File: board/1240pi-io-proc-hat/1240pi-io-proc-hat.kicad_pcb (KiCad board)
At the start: 2 copper layers, 29.2 x 63.5 mm, 12 parts, among them J1 62684-50210, J2 SFV10R-1ST, P445 Header, U445 Z80

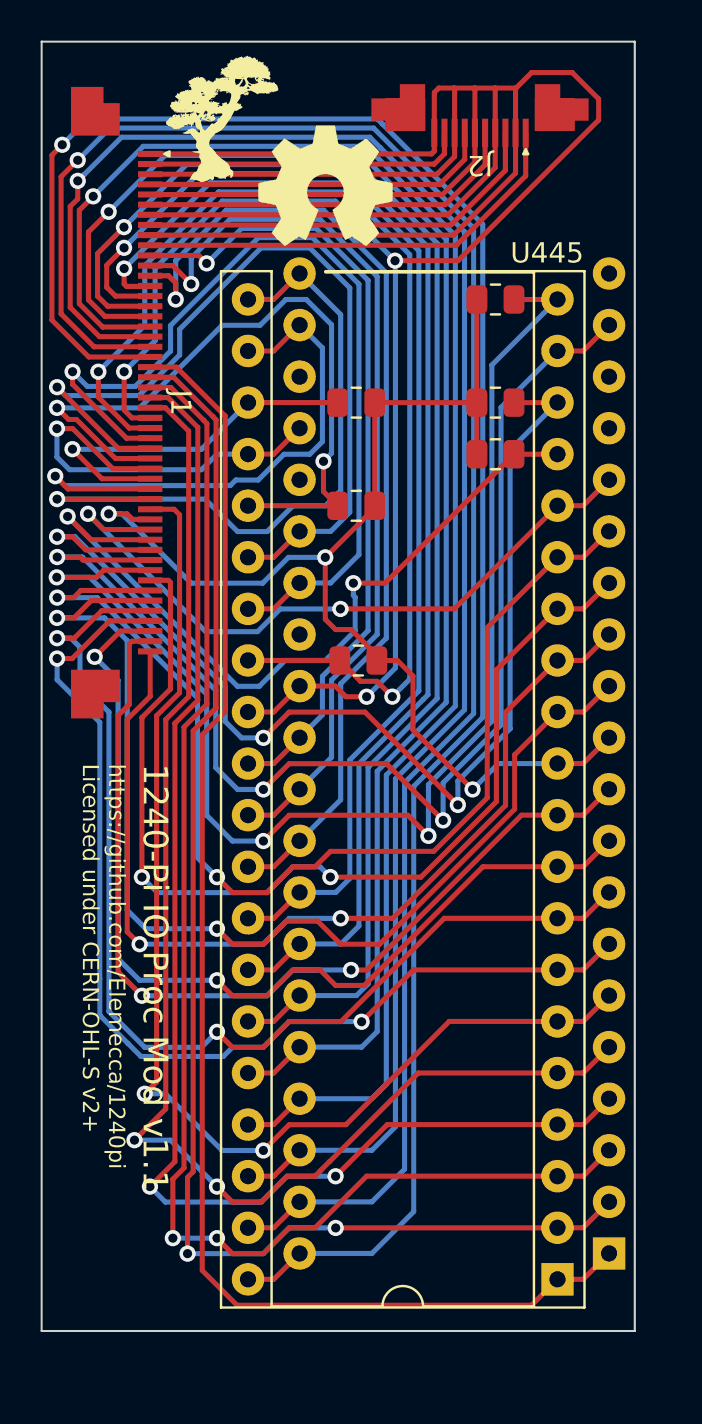
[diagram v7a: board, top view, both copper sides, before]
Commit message: Rearrange IO Proc hat, add IO Proc interface.
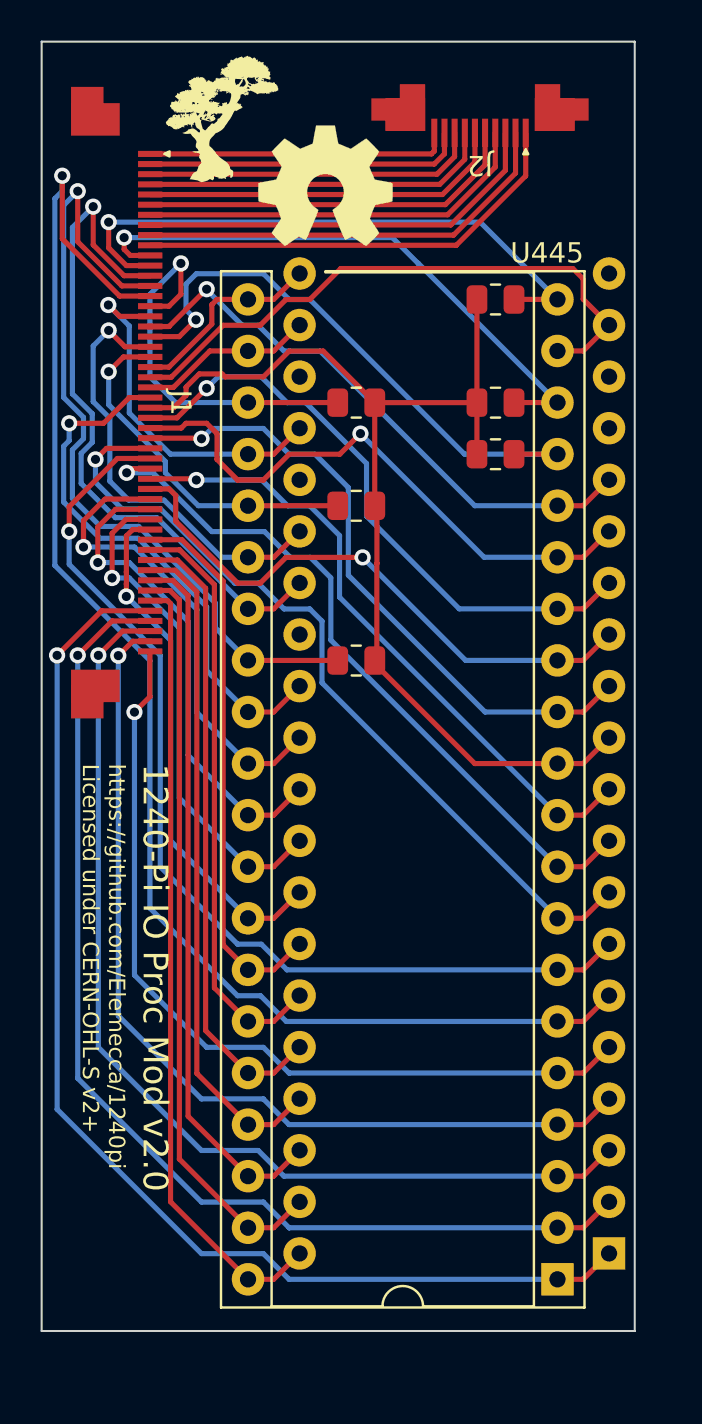
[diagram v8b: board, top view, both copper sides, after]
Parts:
- moved R2 0.10 mm to (150.1, 71.1)
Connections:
- net /~{VDRIVE} renamed /VDRIVE_GREEN
- J1 pad 1: GND -> /VGND5
- J1 pad 11: /A0 -> /~{HALT}
- J1 pad 12: /A1 -> /~{IORQ}
- J1 pad 13: /A2 -> /~{M1}
- J1 pad 14: /A3 -> /~{RFSH}
- J1 pad 15: /A4 -> /~{CLK}
- J1 pad 16: /A5 -> /~{BUSACK}
- J1 pad 17: /A6 -> /~{WAIT}
- J1 pad 18: /A7 -> /~{INT}
- J1 pad 19: /A8 -> /~{NMI}
- J1 pad 20: /A9 -> /~{RESET}
- J1 pad 21: /A10 -> /~{BUSREQ}
- J1 pad 22: /A11 -> /~{RD}
- J1 pad 23: /A12 -> /~{MREQ}
- J1 pad 24: /A13 -> /~{WR}
- J1 pad 25: /A14 -> GND
- J1 pad 26: /A15 -> +5V
- J1 pad 27: GND -> /D0
- J1 pad 28: /~{RFSH} -> /D1
- J1 pad 29: /~{M1} -> /D2
- J1 pad 3: GND -> /VGND4
- J1 pad 30: /~{RESET} -> /D3
- J1 pad 31: /~{BUSRQ} -> /D4
- J1 pad 32: /~{WAIT} -> /D5
- J1 pad 33: /~{BUSACK} -> /D6
- J1 pad 34: /~{WR} -> /D7
- J1 pad 35: /~{RD} -> /A0
- J1 pad 36: /~{CLK} -> /A1
- J1 pad 37: +5V -> /A2
- J1 pad 38: /~{INT} -> /A3
- J1 pad 39: /~{NMI} -> /A4
- J1 pad 40: /~{HALT} -> /A5
- J1 pad 41: /~{MREQ} -> /A6
- J1 pad 42: /~{IORQ} -> /A7
- J1 pad 43: /D0 -> /A8
- J1 pad 44: /D1 -> /A9
- J1 pad 45: /D2 -> /A10
- J1 pad 46: /D3 -> /A11
- J1 pad 47: /D4 -> /A12
- J1 pad 48: /D5 -> /A13
- J1 pad 49: /D6 -> /A14
- J1 pad 5: GND -> /VGND3
- J1 pad 50: /D7 -> /A15
- J1 pad 7: GND -> /VGND2
- J1 pad 9: GND -> /VGND1
- J2 pad 10: GND -> /VGND5
- J2 pad 2: GND -> /VGND1
- J2 pad 4: GND -> /VGND2
- J2 pad 6: GND -> /VGND3
- J2 pad 8: GND -> /VGND4
- R5 pad 1: /~{BUSRQ} -> /~{BUSREQ}
- U445 pad 25: /~{BUSRQ} -> /~{BUSREQ}
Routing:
- net GND: track 176.4 -> 26.8 mm, vias 3 -> 1
- net /A10: track 97.4 -> 39.0 mm, vias 1 -> 0
- net /A9: track 91.8 -> 37.0 mm, vias 1 -> 0
- net /A8: track 86.5 -> 35.1 mm, vias 1 -> 0
- net /A7: track 81.3 -> 33.1 mm, vias 1 -> 0
- net /A6: track 75.2 -> 31.1 mm, vias 1 -> 0
- net /A5: track 69.6 -> 29.1 mm, vias 1 -> 0
- net /A4: track 63.8 -> 27.2 mm, vias 1 -> 0
- net /~{BUSRQ}: track 35.7 -> 0.00 mm, vias 2 -> 0
- net /~{IORQ}: track 64.1 -> 29.5 mm, vias 3 -> 1
- net /A3: track 57.9 -> 25.7 mm
- net /~{MREQ}: track 60.8 -> 29.6 mm, vias 3 -> 0
- net /~{HALT}: track 56.1 -> 28.8 mm, vias 3 -> 1
- net /D1: track 54.8 -> 28.6 mm, vias 2 -> 1
- net /~{RD}: track 34.6 -> 9.83 mm, vias 1 -> 0
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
